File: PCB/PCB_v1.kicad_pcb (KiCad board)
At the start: 2 copper layers, 80 x 40 mm, 9 parts, among them J1 Accelerometer, J2 Flysky FS2A Receiver, J3 DC-DC, J4 Battery Left, J5 Battery Right, J6 ESC_Left, J7 ESC_Right, J8 LED, U1 Teensy4.0

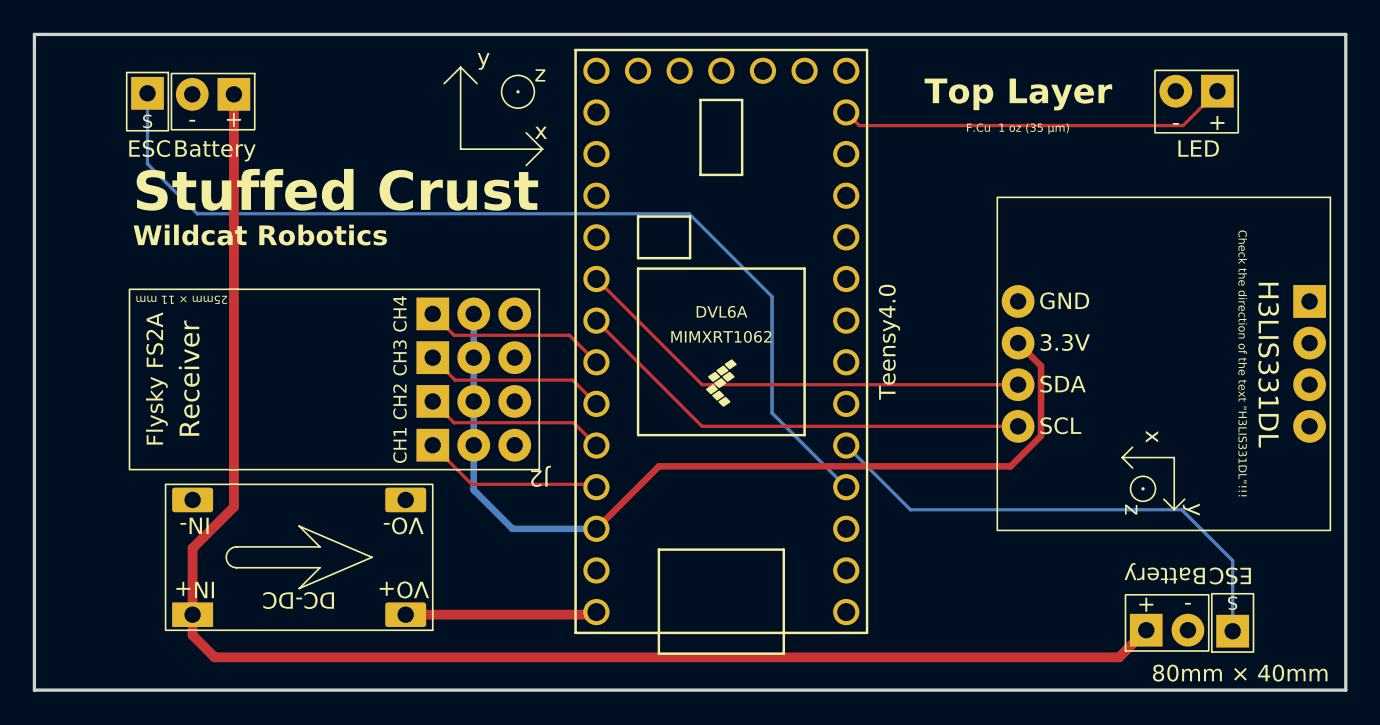
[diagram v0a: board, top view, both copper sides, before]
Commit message: Update PCB Layout (80mm*40mm -> 50mm*40mm)
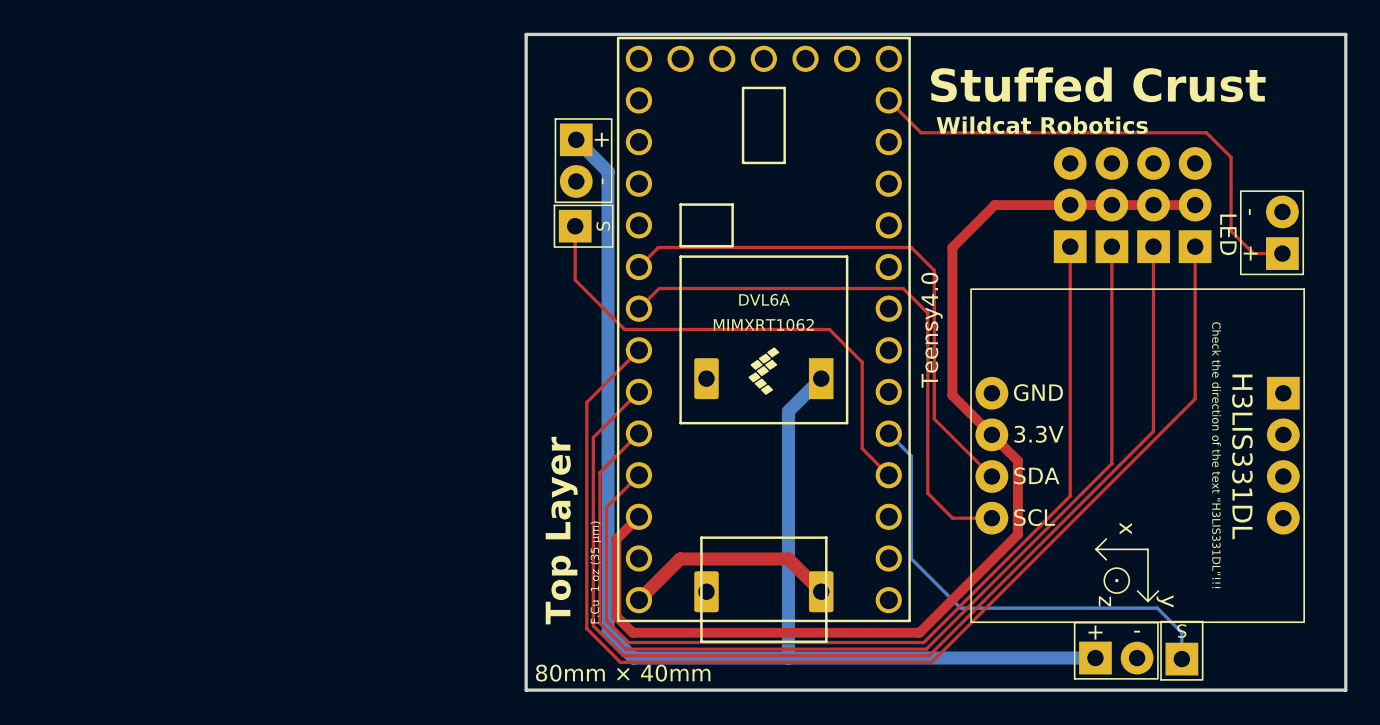
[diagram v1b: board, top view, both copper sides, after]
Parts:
- moved J2 41.3 mm to (207.0, 66.6), turned to -90 degrees
- moved J3 28.7 mm to (184.5, 87.5), turned to 90 degrees
- moved J6 24.9 mm to (171.7, 70.4), turned to 0 degrees
- moved J4 18.6 mm to (171.8, 65.2), turned to 0 degrees
- moved J8 13.1 mm to (217.4, 74.6), turned to 180 degrees
- moved J1 5.82 mm to (217.5, 75.5)
- moved J7 3.54 mm to (208.7, 99.4)
- moved J5 3.54 mm to (203.5, 99.3)
- moved U1 2.70 mm to (184.5, 78.0)
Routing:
- net /CH4_20: track 11.2 -> 72.2 mm
- net /CH3_21: track 11.2 -> 67.3 mm
- net /CH2_22: track 11.1 -> 62.4 mm
- net /CH1_23: track 11.3 -> 57.4 mm
- net /S_ESC_Left_2: track 59.3 -> 30.4 mm
- net /12V: track 93.5 -> 79.1 mm
- net /3.3V: track 54.9 -> 69.1 mm
- net /LED: track 24.1 -> 30.5 mm
- net /SCL_19: track 28.4 -> 34.3 mm
- net /SDA_18: track 28.4 -> 33.1 mm
- net /S_ESC_Right_3: track 30.8 -> 28.9 mm
- net /5V: track 12.2 -> 13.0 mm
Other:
- board size 80 x 40 mm -> 50 x 40 mm
- board text removed: "(PCB Center)"
- board text removed: "Battery"
- board text removed: "ESC"
- board text removed: "z"

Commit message: Finished PCB Layout
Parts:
- moved J4 7.17 mm to (174.1, 71.9), turned to 180 degrees
- moved J6 4.49 mm to (174.2, 66.7), turned to 180 degrees
- moved U1 1.00 mm to (184.5, 79.0)
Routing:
- net /S_ESC_Left_2: track 30.4 -> 38.1 mm
- net /S_ESC_Right_3: track 28.9 -> 24.1 mm
- net /SCL_19: track 34.3 -> 30.8 mm
- net /12V: track 79.1 -> 76.1 mm
- net /SDA_18: track 33.1 -> 31.1 mm
- net /CH4_20: track 72.2 -> 73.6 mm
- net /CH3_21: track 67.3 -> 68.7 mm
- net /CH1_23: track 57.4 -> 58.9 mm
- net /CH2_22: track 62.4 -> 63.8 mm
- net /3.3V: track 69.1 -> 70.5 mm
- net /LED: track 30.5 -> 29.7 mm
- net /5V: track 13.0 -> 12.4 mm
- added copper zone on F.Cu, net /GND
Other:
- board text added: "(Robot Center)"

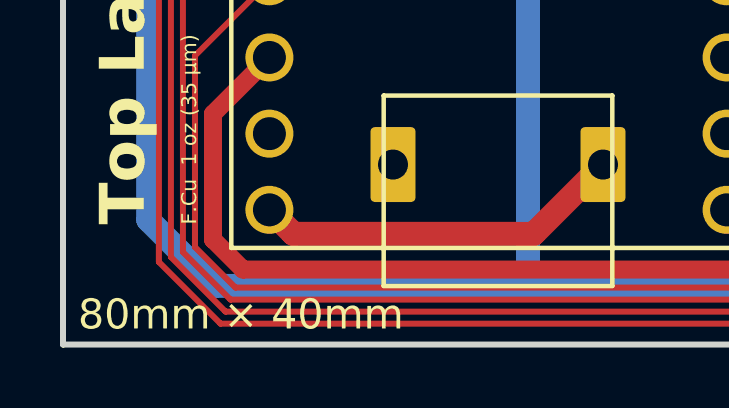
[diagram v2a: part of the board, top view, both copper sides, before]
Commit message: Fix the Text on the PCB
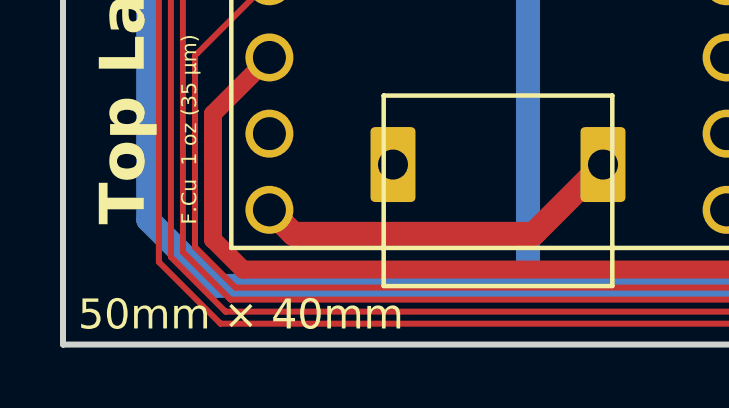
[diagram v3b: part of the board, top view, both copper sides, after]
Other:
- board text added: "50mm × 40mm"
- board text removed: "80mm × 40mm"
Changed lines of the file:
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@@
 		)
 	)
-	(gr_text "80mm × 40mm"
+	(gr_text "50mm × 40mm"
 		(at 170.5 99 0)
 		(layer "F.SilkS")

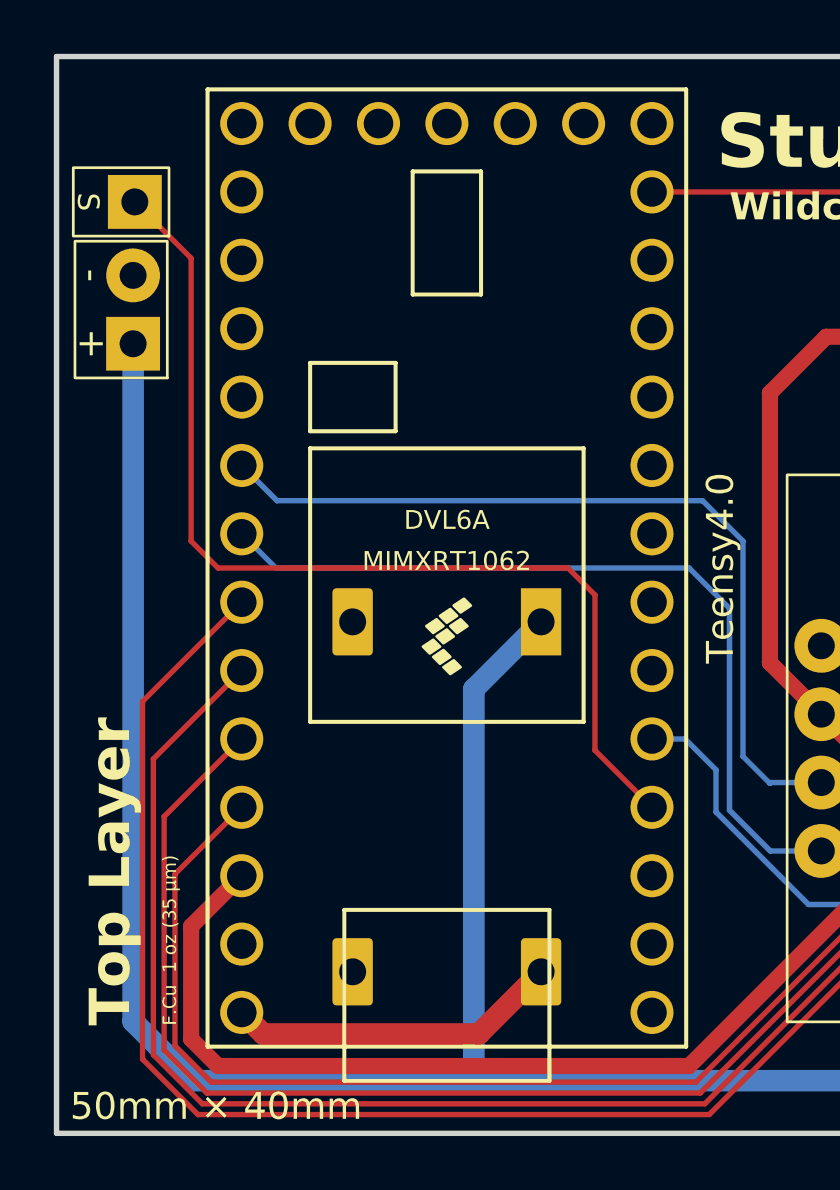
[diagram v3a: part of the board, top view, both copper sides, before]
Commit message: Increase the pad size of Teensy 4.0
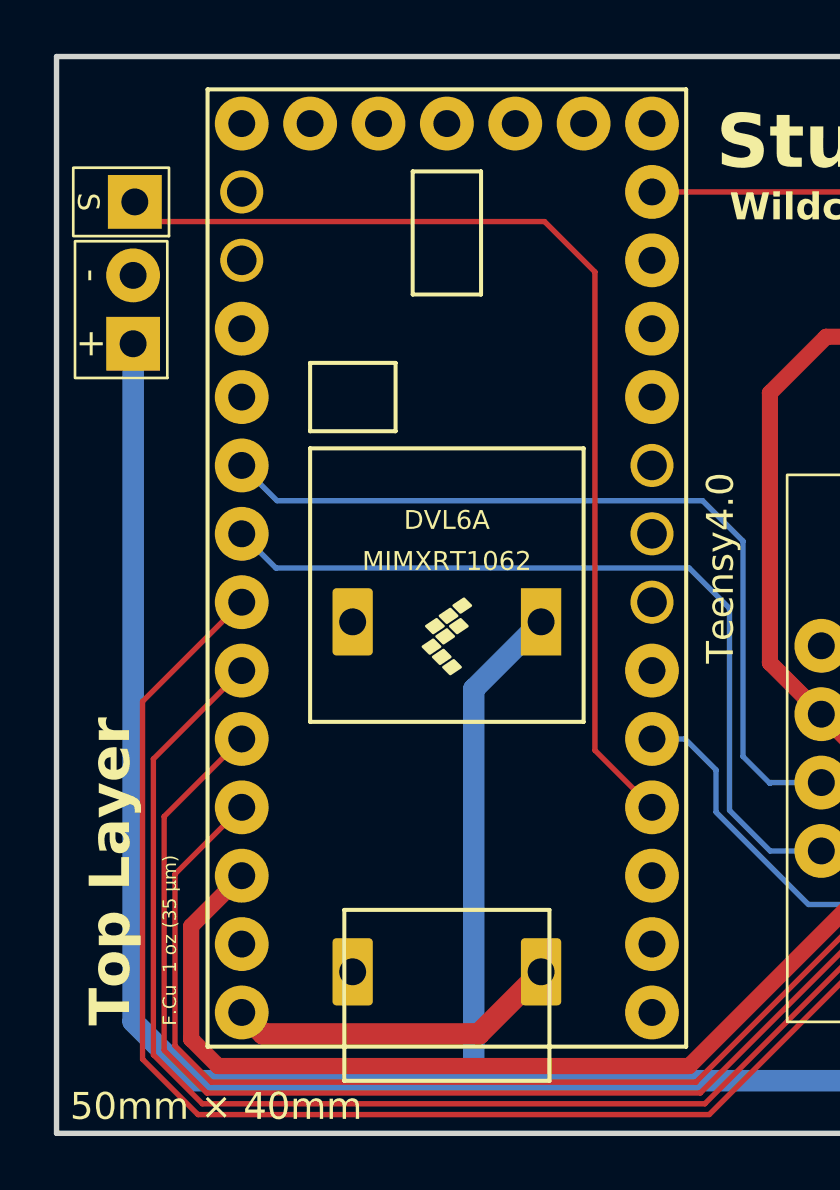
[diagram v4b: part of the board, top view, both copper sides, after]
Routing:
- net /S_ESC_Left_2: track 38.1 -> 38.9 mm
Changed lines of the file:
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@@
 		(pad "1" thru_hole circle
 			(at -16.51 7.62 90)
-			(size 1.6 1.6)
-			(drill 1.1)
+			(size 2 2)
+			(drill 1)
 			(layers "*.Cu" "*.Mask")
 			(remove_unused_layers no)
@@
 		(pad "2" thru_hole circle
 			(at -13.97 7.62 90)
-			(size 1.6 1.6)
-			(drill 1.1)
+			(size 2 2)
+			(drill 1)
 			(layers "*.Cu" "*.Mask")
 			(remove_unused_layers no)
@@
 		(pad "3" thru_hole circle
 			(at -11.43 7.62 90)
-			(size 1.6 1.6)
-			(drill 1.1)
+			(size 2 2)
+			(drill 1)
 			(layers "*.Cu" "*.Mask")
 			(remove_unused_layers no)
@@
 		(pad "4" thru_hole circle
 			(at -8.89 7.62 90)
-			(size 1.6 1.6)
-			(drill 1.1)
+			(size 2 2)
+			(drill 1)
 			(layers "*.Cu" "*.Mask")
 			(remove_unused_layers no)
@@
 		(pad "5" thru_hole circle
 			(at -6.35 7.62 90)
-			(size 1.6 1.6)
-			(drill 1.1)
+			(size 2 2)
+			(drill 1)
 			(layers "*.Cu" "*.Mask")
 			(remove_unused_layers no)
@@
 		(pad "6" thru_hole circle
 			(at -3.81 7.62 90)
-			(size 1.6 1.6)
-			(drill 1.1)
+			(size 2 2)
+			(drill 1)
 			(layers "*.Cu" "*.Mask")
 			(remove_unused_layers no)
@@
 		(pad "10" thru_hole circle
 			(at 6.35 7.62 90)
-			(size 1.6 1.6)
-			(drill 1.1)
+			(size 2 2)
+			(drill 1)
 			(layers "*.Cu" "*.Mask")
 			(remove_unused_layers no)
@@
 		(pad "11" thru_hole circle
 			(at 8.89 7.62 90)
-			(size 1.6 1.6)
-			(drill 1.1)
+			(size 2 2)
+			(drill 1)
 			(layers "*.Cu" "*.Mask")
 			(remove_unused_layers no)
@@
 		(pad "12" thru_hole circle
 			(at 11.43 7.62 90)
-			(size 1.6 1.6)
-			(drill 1.1)
+			(size 2 2)
+			(drill 1)
 			(layers "*.Cu" "*.Mask")
 			(remove_unused_layers no)
@@
 		(pad "13" thru_hole circle
 			(at 13.97 7.62 90)
-			(size 1.6 1.6)
-			(drill 1.1)
+			(size 2 2)
+			(drill 1)
 			(layers "*.Cu" "*.Mask")
 			(remove_unused_layers no)
@@
 		(pad "14" thru_hole circle
 			(at 16.51 7.62 90)
-			(size 1.6 1.6)
-			(drill 1.1)
+			(size 2 2)
+			(drill 1)
 			(layers "*.Cu" "*.Mask")
 			(remove_unused_layers no)
@@
 		(pad "15" thru_hole circle
 			(at 16.51 5.08 90)
-			(size 1.6 1.6)
-			(drill 1.1)
+			(size 2 2)
+			(drill 1)
 			(layers "*.Cu" "*.Mask")
 			(remove_unused_layers no)
@@
 		(pad "16" thru_hole circle
 			(at 16.51 2.54 90)
-			(size 1.6 1.6)
-			(drill 1.1)
+			(size 2 2)
+			(drill 1)
 			(layers "*.Cu" "*.Mask")
 			(remove_unused_layers no)
@@
 		(pad "17" thru_hole circle
 			(at 16.51 0 90)
-			(size 1.6 1.6)
-			(drill 1.1)
+			(size 2 2)
+			(drill 1)
 			(layers "*.Cu" "*.Mask")
 			(remove_unused_layers no)
@@
 		(pad "18" thru_hole circle
 			(at 16.51 -2.54 90)
-			(size 1.6 1.6)
-			(drill 1.1)
+			(size 2 2)
+			(drill 1)
 			(layers "*.Cu" "*.Mask")
 			(remove_unused_layers no)
@@
 		(pad "19" thru_hole circle
 			(at 16.51 -5.08 90)
-			(size 1.6 1.6)
-			(drill 1.1)
+			(size 2 2)
+			(drill 1)
 			(layers "*.Cu" "*.Mask")
 			(remove_unused_layers no)
@@
 		(pad "20" thru_hole circle
 			(at 16.51 -7.62 90)
-			(size 1.6 1.6)
-			(drill 1.1)
+			(size 2 2)
+			(drill 1)
 			(layers "*.Cu" "*.Mask")
 			(remove_unused_layers no)
@@
 		(pad "23" thru_hole circle
 			(at 8.89 -7.62 90)
-			(size 1.6 1.6)
-			(drill 1.1)
+			(size 2 2)
+			(drill 1)
 			(layers "*.Cu" "*.Mask")
 			(remove_unused_layers no)
@@
 		(pad "24" thru_hole circle
 			(at 6.35 -7.62 90)
-			(size 1.6 1.6)
-			(drill 1.1)
+			(size 2 2)
+			(drill 1)
 			(layers "*.Cu" "*.Mask")
 			(remove_unused_layers no)
@@
 		(pad "25" thru_hole circle
 			(at 3.81 -7.62 90)
-			(size 1.6 1.6)
-			(drill 1.1)
+			(size 2 2)
+			(drill 1)
 			(layers "*.Cu" "*.Mask")
 			(remove_unused_layers no)
@@
 		(pad "26" thru_hole circle
 			(at 1.27 -7.62 90)
-			(size 1.6 1.6)
-			(drill 1.1)
+			(size 2 2)
+			(drill 1)
 			(layers "*.Cu" "*.Mask")
 			(remove_unused_layers no)
@@
 		(pad "27" thru_hole circle
 			(at -1.27 -7.62 90)
-			(size 1.6 1.6)
-			(drill 1.1)
+			(size 2 2)
+			(drill 1)
 			(layers "*.Cu" "*.Mask")
 			(remove_unused_layers no)
@@
 		(pad "28" thru_hole circle
 			(at -3.81 -7.62 90)
-			(size 1.6 1.6)
-			(drill 1.1)
+			(size 2 2)
+			(drill 1)
 			(layers "*.Cu" "*.Mask")
 			(remove_unused_layers no)
@@
 		(pad "29" thru_hole circle
 			(at -6.35 -7.62 90)
-			(size 1.6 1.6)
-			(drill 1.1)
+			(size 2 2)
+			(drill 1)
 			(layers "*.Cu" "*.Mask")
 			(remove_unused_layers no)
@@
 		(pad "30" thru_hole circle
 			(at -8.89 -7.62 90)
-			(size 1.6 1.6)
-			(drill 1.1)
+			(size 2 2)
+			(drill 1)
 			(layers "*.Cu" "*.Mask")
 			(remove_unused_layers no)
@@
 		(pad "31" thru_hole circle
 			(at -11.43 -7.62 90)
-			(size 1.6 1.6)
-			(drill 1.1)
+			(size 2 2)
+			(drill 1)
 			(layers "*.Cu" "*.Mask")
 			(remove_unused_layers no)
@@
 		(pad "32" thru_hole circle
 			(at -13.97 -7.62 90)
-			(size 1.6 1.6)
-			(drill 1.1)
+			(size 2 2)
+			(drill 1)
 			(layers "*.Cu" "*.Mask")
 			(remove_unused_layers no)
@@
 		(pad "33" thru_hole circle
 			(at -16.51 -7.62 90)
-			(size 1.6 1.6)
-			(drill 1.1)
+			(size 2 2)
+			(drill 1)
 			(layers "*.Cu" "*.Mask")
 			(remove_unused_layers no)
@@
 	)
 	(segment
-		(start 175 67.492)
-		(end 172.908 65.4)
+		(start 172.908 65.4)
+		(end 173.639 66.131)
 		(width 0.2)
 		(layer "F.Cu")
@@
 	)
 	(segment
-		(start 190 80)
-		(end 189 79)
-		(width 0.2)
-		(layer "F.Cu")
-		(net 11)
-	)
-	(segment
-		(start 176 79)
-		(end 175 78)
-		(width 0.2)
-		(layer "F.Cu")
-		(net 11)
-	)
-	(segment
-		(start 189 79)
-		(end 176 79)
-		(width 0.2)
-		(layer "F.Cu")
-		(net 11)
-	)
-	(segment
-		(start 190 85.77)
-		(end 190 80)
-		(width 0.2)
-		(layer "F.Cu")
-		(net 11)
-	)
-	(segment
-		(start 192.12 87.89)
+		(start 190 68)
 		(end 190 85.77)
 		(width 0.2)
@@
 	)
 	(segment
-		(start 175 78)
-		(end 175 67.492)
+		(start 188.131 66.131)
+		(end 190 68)
 		(width 0.2)
 		(layer "F.Cu")
+		(net 11)
+	)
+	(segment
+		(start 190 85.77)
+		(end 192.12 87.89)
+		(width 0.2)
+		(layer "F.Cu")
+		(net 11)
+	)
+	(segment
+		(start 173.639 66.131)
+		(end 188.131 66.131)
+		(width 0.2)
+		(layer "F.Cu")
